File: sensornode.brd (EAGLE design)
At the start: 112.3 x 63.5 mm, 75 parts, among them IC1 CP2104, Q1 mmbt2222, Q2 mmbt2222, Q3 DMG3415U, SW2 KMR2, U1 TSL2591, U2 AP2112-3.3, U3 MCP73831T-2ACI/OT, U4 BMEx80, X2 ESP32_WROOM32_SKINNY, X4 20329

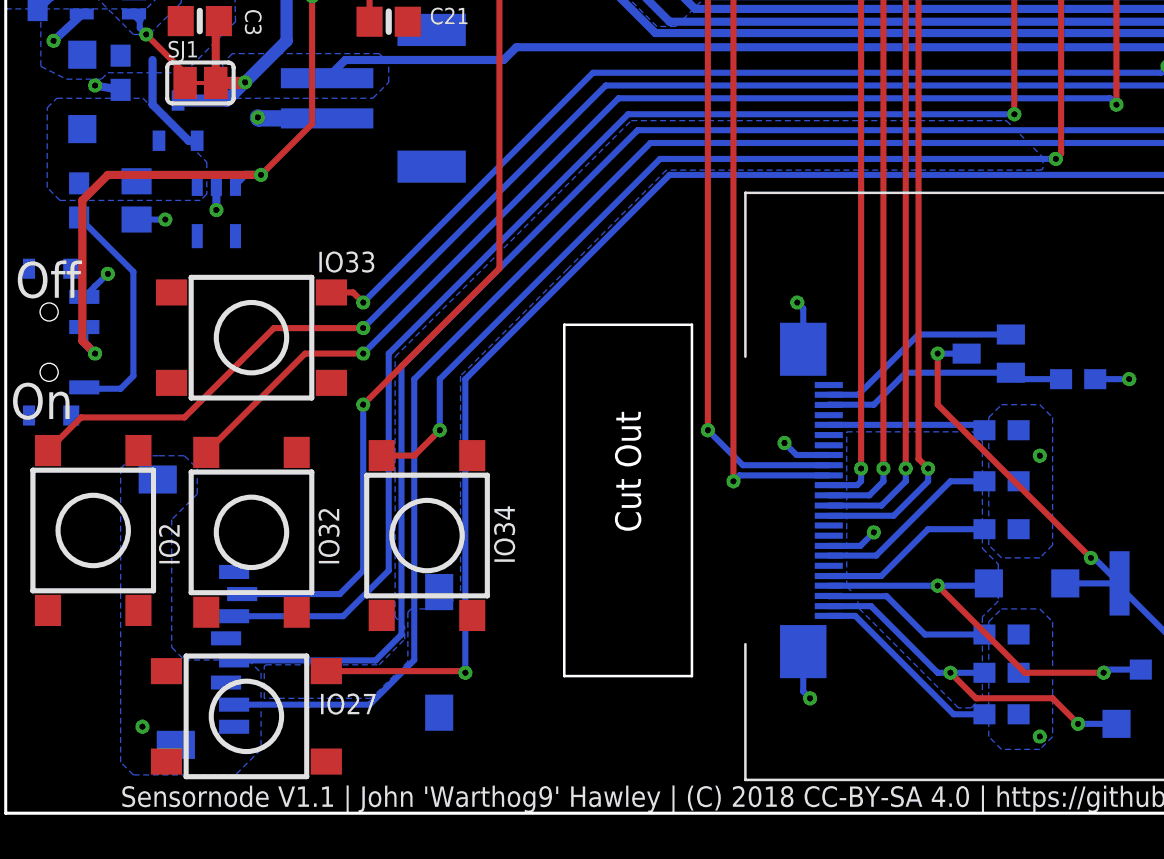
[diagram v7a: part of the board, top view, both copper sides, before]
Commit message: Swapping out microSD cage for the Molex
The 4UConn cage is delightlyfully cheap, but the lead times are
dicey.  At least for this run I'm going to go with the easily
found, but more expensive, card cage, and I'll revert when
I've got more time on a different production run.
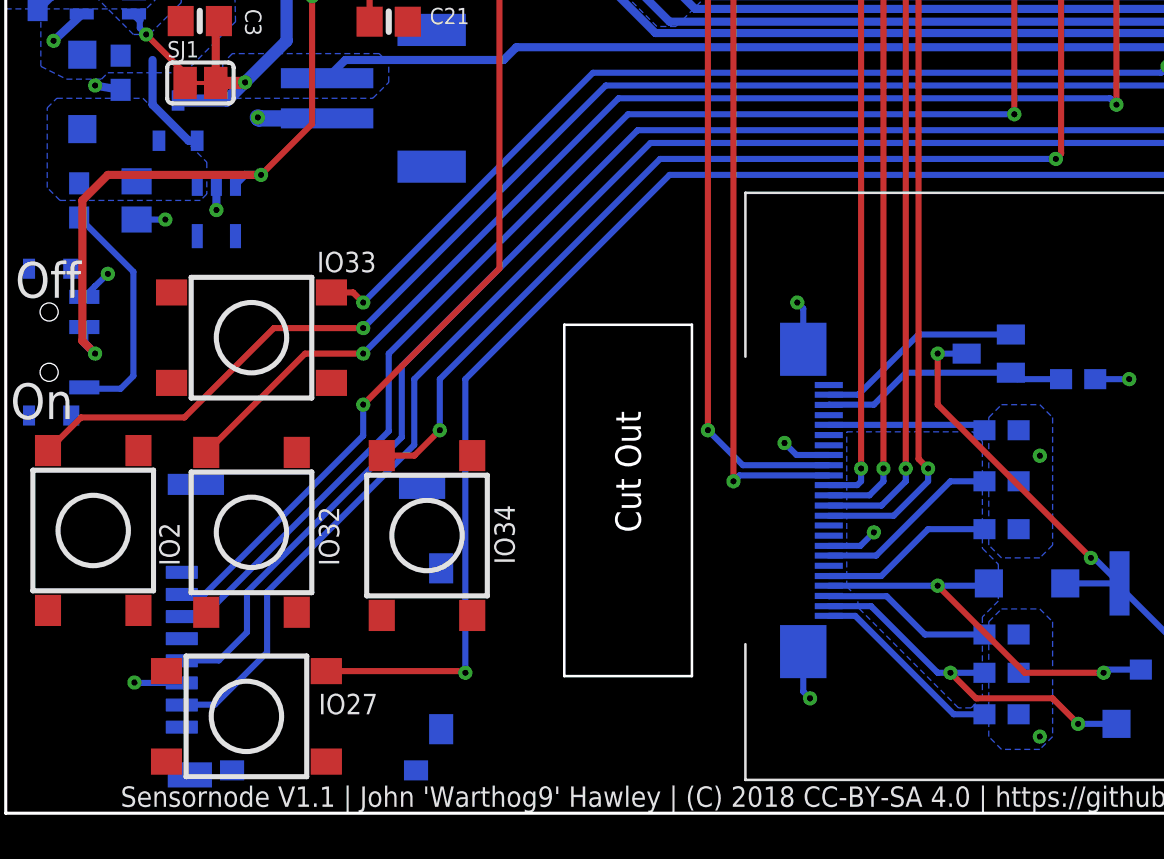
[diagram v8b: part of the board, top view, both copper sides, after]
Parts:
- removed U$17: MICROSD, adafruit:MICROSD
- added SD1: SD-CARD-MSD50, we-con:SD_5031821853
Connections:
- net 3.3V: now also SD1.VCC; no longer U$17.4
- net GND: now also SD1.GND; no longer U$17.6, U$17.MT1, U$17.MT2
- net HSPI_CS0-IO15_A8: now also SD1.CS; no longer U$17.2
- net HSPI_MISO-IO12_A11: now also SD1.MISO; no longer U$17.7
- net HSPI_MOSI-IO13_A12: now also SD1.MOSI; no longer U$17.3
- net HSPI_SCLK-IO14_A6: now also SD1.SCK; no longer U$17.5
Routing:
- net GND: track 28.5 -> 30.9 mm
- net HSPI_SCLK-IO14_A6: track 124.1 -> 122.1 mm
- net HSPI_MISO-IO12_A11: track 123.4 -> 121.5 mm
- net HSPI_MOSI-IO13_A12: track 119.0 -> 117.5 mm
- net HSPI_CS0-IO15_A8: track 126.9 -> 125.9 mm
- removed copper zone on layer 16, net N$27
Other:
- board text added: "Sensornode V1.1 John 'Warthog9' Hawley | (C) 2018 CC-BY-SA 4.0 https://github.com/unreproducible/sensornode"
